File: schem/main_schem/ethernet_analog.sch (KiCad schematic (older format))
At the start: 11 parts

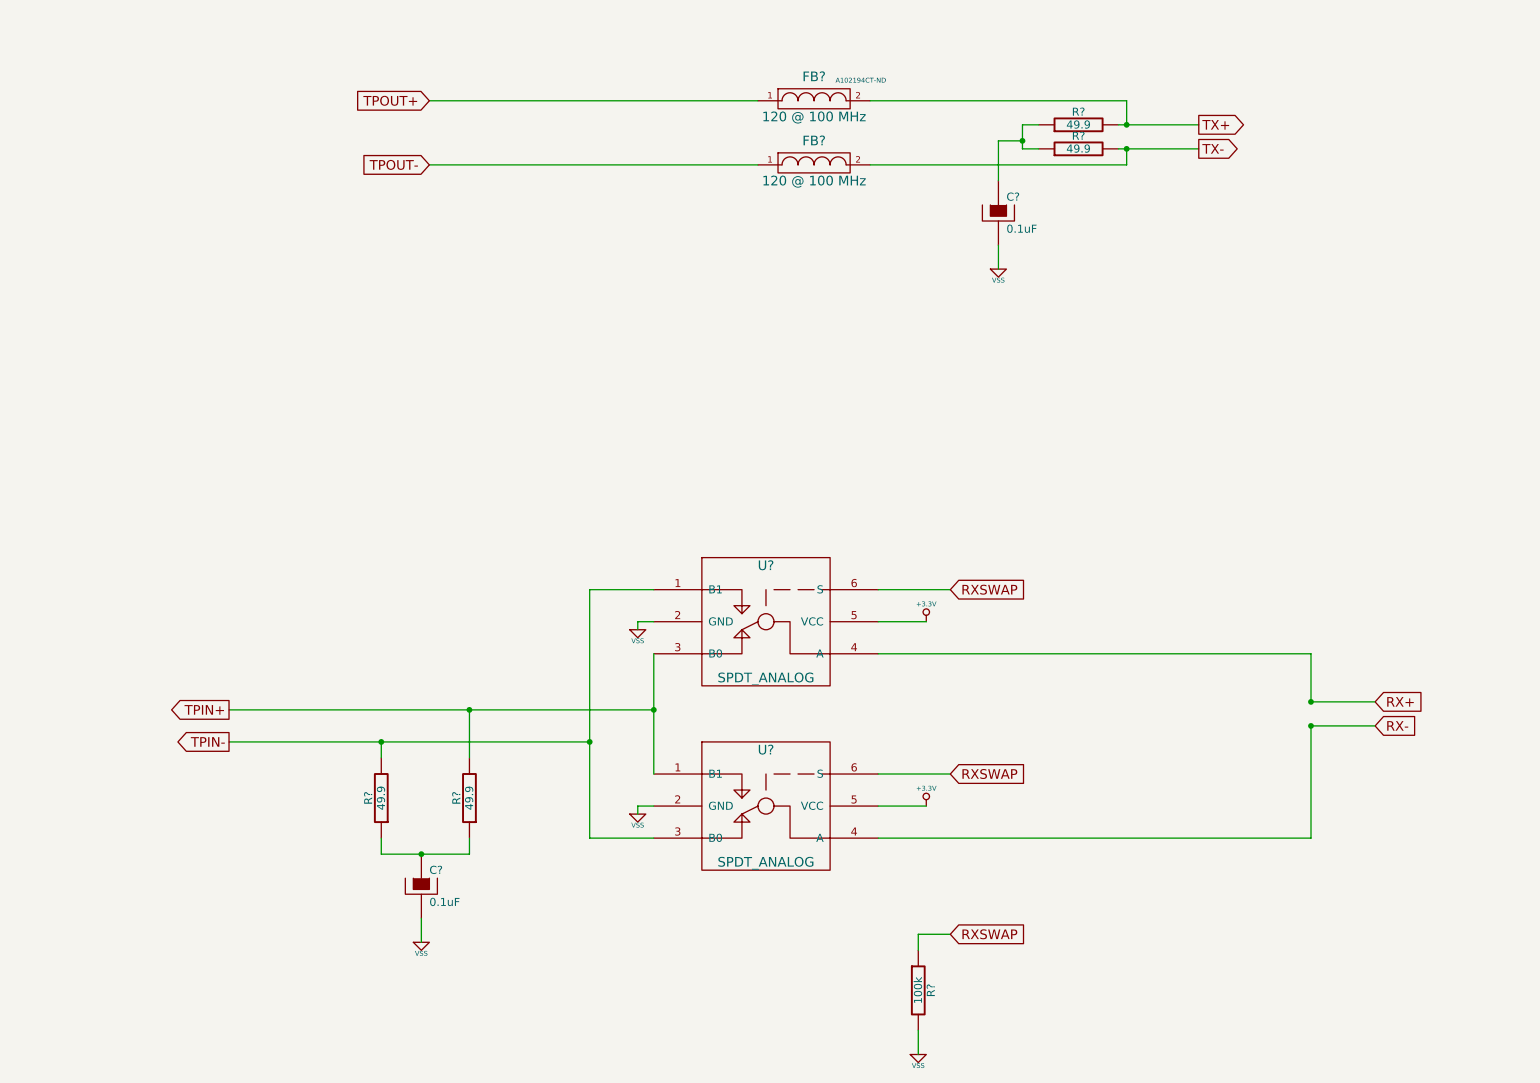
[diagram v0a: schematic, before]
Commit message: BOM sheets, update ethernet analog circuit
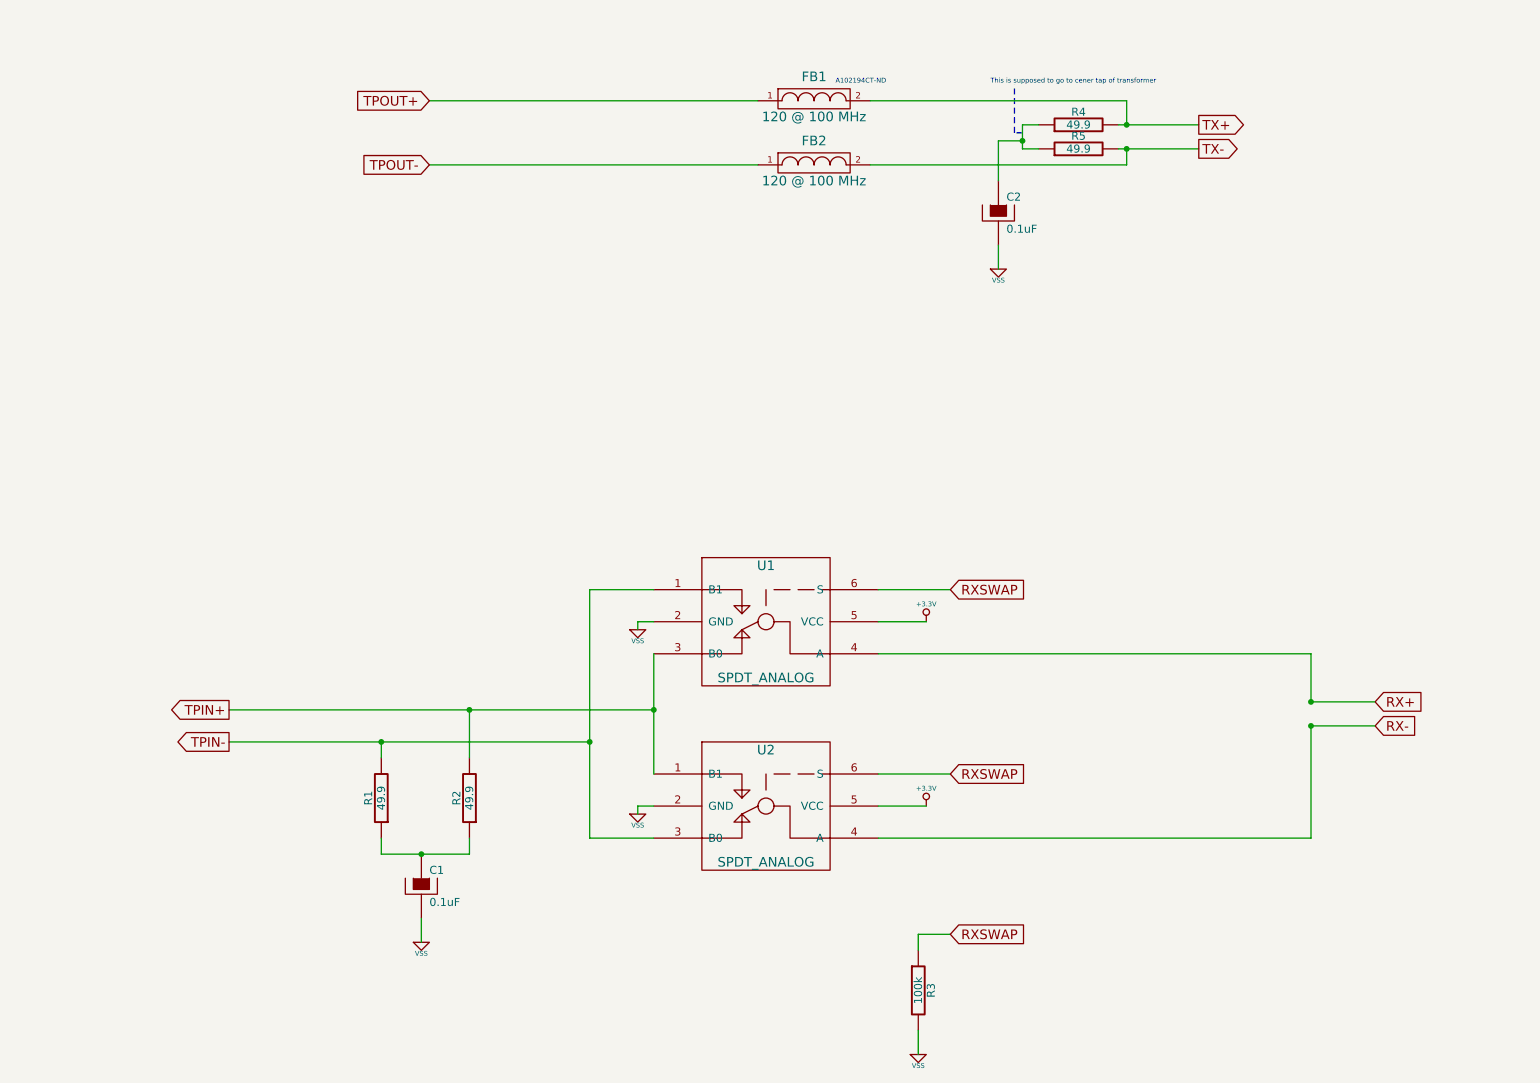
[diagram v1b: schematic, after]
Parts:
- gave numbers to parts that had none: 11
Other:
- note added: "This is supposed to go to cener tap of transformer"
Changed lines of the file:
@@
-EESchema Schematic File Version 2  date 10/5/2012 10:31:23 AM
+EESchema Schematic File Version 2  date 10/5/2012 11:52:46 PM
 LIBS:power
 LIBS:device
@@
 encoding utf-8
 Sheet 2 6
-Title ""
-Date "5 oct 2012"
+Title "Ethernet Analog Subsystem w/ Polarity Switching"
+Date "6 oct 2012"
 Rev ""
-Comp ""
-Comment1 ""
+Comp "Ingersoll Rand 402 Group"
+Comment1 "Brock Anderson, 2012"
 Comment2 ""
 Comment3 ""
 Comment4 ""
 $EndDescr
-$Comp
-L VSS #PWR?
+Wire Notes Line
+	7450 1250 7400 1250
+Wire Notes Line
+	7400 1250 7400 950
+Connection ~ 3700 5750
+Wire Wire Line
+	4000 5650 4000 5750
+Wire Wire Line
+	4000 5750 3450 5750
+Connection ~ 4000 4850
+Wire Wire Line
+	4000 5150 4000 4850
+Wire Wire Line
+	9650 4950 9250 4950
+Connection ~ 4750 5050
+Wire Wire Line
+	5150 4100 4750 4100
+Wire Wire Line
+	4750 4100 4750 5650
+Connection ~ 5150 4850
+Wire Wire Line
+	5150 5250 5150 4500
+Connection ~ 9250 4950
+Wire Wire Line
+	9250 4950 9250 5650
+Wire Wire Line
+	9250 5650 6550 5650
+Wire Wire Line
+	7000 6250 6800 6250
+Wire Wire Line
+	6800 6250 6800 6350
+Wire Wire Line
+	6550 5250 7000 5250
+Wire Wire Line
+	5050 4350 5050 4300
+Wire Wire Line
+	5050 4300 5150 4300
+Wire Wire Line
+	6550 5450 6850 5450
+Connection ~ 7450 1300
+Wire Wire Line
+	7450 1200 7450 1350
+Wire Wire Line
+	7450 1200 7550 1200
+Wire Wire Line
+	7300 1950 7300 2100
+Wire Wire Line
+	3750 1450 5800 1450
+Connection ~ 8100 1200
+Wire Wire Line
+	8100 1200 8100 1050
+Wire Wire Line
+	8100 1050 6500 1050
+Wire Wire Line
+	8050 1200 8550 1200
+Wire Wire Line
+	8050 1350 8550 1350
+Wire Wire Line
+	6500 1450 8100 1450
+Wire Wire Line
+	8100 1450 8100 1350
+Connection ~ 8100 1350
+Wire Wire Line
+	3750 1050 5800 1050
+Wire Wire Line
+	7300 1550 7300 1300
+Wire Wire Line
+	7300 1300 7450 1300
+Wire Wire Line
+	7450 1350 7550 1350
+Wire Wire Line
+	6550 4300 6850 4300
+Wire Wire Line
+	5050 5500 5050 5450
+Wire Wire Line
+	5050 5450 5150 5450
+Wire Wire Line
+	6550 4100 7000 4100
+Wire Wire Line
+	6800 6850 6800 7000
+Wire Wire Line
+	6550 4500 9250 4500
+Wire Wire Line
+	9250 4500 9250 4800
+Connection ~ 9250 4800
+Wire Wire Line
+	5150 4850 2500 4850
+Wire Wire Line
+	4750 5050 2500 5050
+Wire Wire Line
+	4750 5650 5150 5650
+Wire Wire Line
+	9250 4800 9650 4800
+Wire Wire Line
+	3450 5150 3450 5050
+Connection ~ 3450 5050
+Wire Wire Line
+	3450 5750 3450 5650
+Wire Wire Line
+	3700 6150 3700 6300
+Text Notes 7250 950  0    30   ~ 0
+This is supposed to go to cener tap of transformer
+$Comp
+L VSS #PWR01
 U 1 1 506EFD34
 P 7300 2100
-F 0 "#PWR?" H 7300 2100 30  0001 C CNN
+F 0 "#PWR01" H 7300 2100 30  0001 C CNN
 F 1 "VSS" H 7300 2030 30  0000 C CNN
 	1    7300 2100
 	1    0    0    -1
 $EndComp
-Wire Wire Line
-	3700 6150 3700 6300
-Wire Wire Line
-	3450 5650 3450 5750
-Connection ~ 3450 5050
-Wire Wire Line
-	3450 5150 3450 5050
-Wire Wire Line
-	9650 4800 9250 4800
-Wire Wire Line
-	5150 5650 4750 5650
-Wire Wire Line
-	4750 5050 2500 5050
-Wire Wire Line
-	5150 4850 2500 4850
-Connection ~ 9250 4800
-Wire Wire Line
-	9250 4800 9250 4500
-Wire Wire Line
-	9250 4500 6550 4500
-Wire Wire Line
-	6800 6850 6800 7000
-Wire Wire Line
-	6550 4100 7000 4100
-Wire Wire Line
-	5150 5450 5050 5450
-Wire Wire Line
-	5050 5450 5050 5500
-Wire Wire Line
-	6550 4300 6850 4300
-Wire Wire Line
-	7550 1350 7450 1350
-Wire Wire Line
-	7450 1300 7300 1300
-Wire Wire Line
-	7300 1300 7300 1550
-Wire Wire Line
-	3750 1050 5800 1050
-Connection ~ 8100 1350
-Wire Wire Line
-	8100 1350 8100 1450
-Wire Wire Line
-	8100 1450 6500 1450
-Wire Wire Line
-	8050 1350 8550 1350
-Wire Wire Line
-	8050 1200 8550 1200
-Wire Wire Line
-	6500 1050 8100 1050
-Wire Wire Line
-	8100 1050 8100 1200
-Connection ~ 8100 1200
-Wire Wire Line
-	3750 1450 5800 1450
-Wire Wire Line
-	7300 1950 7300 2100
-Wire Wire Line
-	7550 1200 7450 1200
-Wire Wire Line
-	7450 1200 7450 1350
-Connection ~ 7450 1300
-Wire Wire Line
-	6550 5450 6850 5450
-Wire Wire Line
-	5150 4300 5050 4300
-Wire Wire Line
-	5050 4300 5050 4350
-Wire Wire Line
-	6550 5250 7000 5250
-Wire Wire Line
-	6800 6350 6800 6250
-Wire Wire Line
-	6800 6250 7000 6250
-Wire Wire Line
-	6550 5650 9250 5650
-Wire Wire Line
-	9250 5650 9250 4950
-Connection ~ 9250 4950
-Wire Wire Line
-	5150 5250 5150 4500
-Connection ~ 5150 4850
-Wire Wire Line
-	4750 5650 4750 4100
-Wire Wire Line
-	4750 4100 5150 4100
-Connection ~ 4750 5050
-Wire Wire Line
-	9250 4950 9650 4950
-Wire Wire Line
-	4000 5150 4000 4850
-Connection ~ 4000 4850
-Wire Wire Line
-	3450 5750 4000 5750
-Wire Wire Line
-	4000 5750 4000 5650
-Connection ~ 3700 5750
-$Comp
-L CP C?
+$Comp
+L CP C1
 U 1 1 506EFD16
 P 3700 5950
-F 0 "C?" H 3750 6050 50  0000 L CNN
+F 0 "C1" H 3750 6050 50  0000 L CNN
 F 1 "0.1uF" H 3750 5850 50  0000 L CNN
 	1    3700 5950
@@
 $EndComp
 $Comp
-L VSS #PWR?
+L VSS #PWR02
 U 1 1 506EFD0E
 P 3700 6300
-F 0 "#PWR?" H 3700 6300 30  0001 C CNN
+F 0 "#PWR02" H 3700 6300 30  0001 C CNN
 F 1 "VSS" H 3700 6230 30  0000 C CNN
 	1    3700 6300
@@
 $EndComp
 $Comp
-L VSS #PWR?
+L VSS #PWR03
 U 1 1 506EFADF
 P 6800 7000
-F 0 "#PWR?" H 6800 7000 30  0001 C CNN
+F 0 "#PWR03" H 6800 7000 30  0001 C CNN
 F 1 "VSS" H 6800 6930 30  0000 C CNN
 	1    6800 7000
@@
 $EndComp
 $Comp
-L R R?
+L R R3
 U 1 1 506EFAD8
 P 6800 6600
-F 0 "R?" V 6880 6600 50  0000 C CNN
+F 0 "R3" V 6880 6600 50  0000 C CNN
 F 1 "100k" V 6800 6600 50  0000 C CNN
 	1    6800 6600
@@
 RXSWAP
 $Comp
-L VSS #PWR?
+L VSS #PWR04
 U 1 1 506EFA1F
 P 5050 4350
-F 0 "#PWR?" H 5050 4350 30  0001 C CNN
+F 0 "#PWR04" H 5050 4350 30  0001 C CNN
 F 1 "VSS" H 5050 4280 30  0000 C CNN
 	1    5050 4350
@@
 $EndComp
 $Comp
-L VSS #PWR?
+L VSS #PWR05
 U 1 1 506EF9D4
 P 5050 5500
-F 0 "#PWR?" H 5050 5500 30  0001 C CNN
+F 0 "#PWR05" H 5050 5500 30  0001 C CNN
 F 1 "VSS" H 5050 5430 30  0000 C CNN
 	1    5050 5500
@@
 $EndComp
 $Comp
-L +3.3V #PWR?
+L +3.3V #PWR06
 U 1 1 506EF9AE
 P 6850 5450
-F 0 "#PWR?" H 6850 5410 30  0001 C CNN
+F 0 "#PWR06" H 6850 5410 30  0001 C CNN
 F 1 "+3.3V" H 6850 5560 30  0000 C CNN
 	1    6850 5450
@@
 $EndComp
 $Comp
-L +3.3V #PWR?
+L +3.3V #PWR07
 U 1 1 506EF99F
 P 6850 4300
-F 0 "#PWR?" H 6850 4260 30  0001 C CNN
+F 0 "#PWR07" H 6850 4260 30  0001 C CNN
 F 1 "+3.3V" H 6850 4410 30  0000 C CNN
 	1    6850 4300
@@
 $EndComp
 $Comp
-L SPDT_ANALOG U?
+L SPDT_ANALOG U2
 U 1 1 506EF954
 P 5850 5400
-F 0 "U?" H 5850 5700 60  0000 C CNN
+F 0 "U2" H 5850 5700 60  0000 C CNN
 F 1 "SPDT_ANALOG" H 5850 5000 60  0000 C CNN
 	1    5850 5400
@@
 $EndComp
 $Comp
-L SPDT_ANALOG U?
+L SPDT_ANALOG U1
 U 1 1 506EF94B
 P 5850 4250
-F 0 "U?" H 5850 4550 60  0000 C CNN
+F 0 "U1" H 5850 4550 60  0000 C CNN
 F 1 "SPDT_ANALOG" H 5850 3850 60  0000 C CNN
 	1    5850 4250
@@
 $EndComp
 $Comp
-L CP C?
+L CP C2
 U 1 1 506EF466
 P 7300 1750
-F 0 "C?" H 7350 1850 50  0000 L CNN
+F 0 "C2" H 7350 1850 50  0000 L CNN
 F 1 "0.1uF" H 7350 1650 50  0000 L CNN
 	1    7300 1750
@@
 A102194CT-ND
 $Comp
-L FILTER FB?
+L FILTER FB2
 U 1 1 506EF3B9
 P 6150 1450
-F 0 "FB?" H 6150 1600 60  0000 C CNN
+F 0 "FB2" H 6150 1600 60  0000 C CNN
 F 1 "120 @ 100 MHz" H 6150 1350 60  0000 C CNN
 	1    6150 1450
@@
 $EndComp
 $Comp
-L FILTER FB?
+L FILTER FB1
 U 1 1 506EF3AF
 P 6150 1050
-F 0 "FB?" H 6150 1200 60  0000 C CNN
+F 0 "FB1" H 6150 1200 60  0000 C CNN
 F 1 "120 @ 100 MHz" H 6150 950 60  0000 C CNN
 	1    6150 1050
@@
 $EndComp
 $Comp
-L R R?
+L R R5
 U 1 1 506EEDA5
 P 7800 1350
-F 0 "R?" V 7880 1350 50  0000 C CNN
+F 0 "R5" V 7880 1350 50  0000 C CNN
 F 1 "49.9" V 7800 1350 50  0000 C CNN
 	1    7800 1350
@@
 $EndComp
 $Comp
-L R R?
+L R R4
 U 1 1 506EED9D
 P 7800 1200
-F 0 "R?" V 7880 1200 50  0000 C CNN
+F 0 "R4" V 7880 1200 50  0000 C CNN
 F 1 "49.9" V 7800 1200 50  0000 C CNN
 	1    7800 1200
@@
 $EndComp
 $Comp
-L R R?
+L R R2
 U 1 1 506EED96
 P 4000 5400
-F 0 "R?" V 4080 5400 50  0000 C CNN
+F 0 "R2" V 4080 5400 50  0000 C CNN
 F 1 "49.9" V 4000 5400 50  0000 C CNN
 	1    4000 5400
@@
 $EndComp
 $Comp
-L R R?
+L R R1
 U 1 1 506EED8E
 P 3450 5400
-F 0 "R?" V 3530 5400 50  0000 C CNN
+F 0 "R1" V 3530 5400 50  0000 C CNN
 F 1 "49.9" V 3450 5400 50  0000 C CNN
 	1    3450 5400

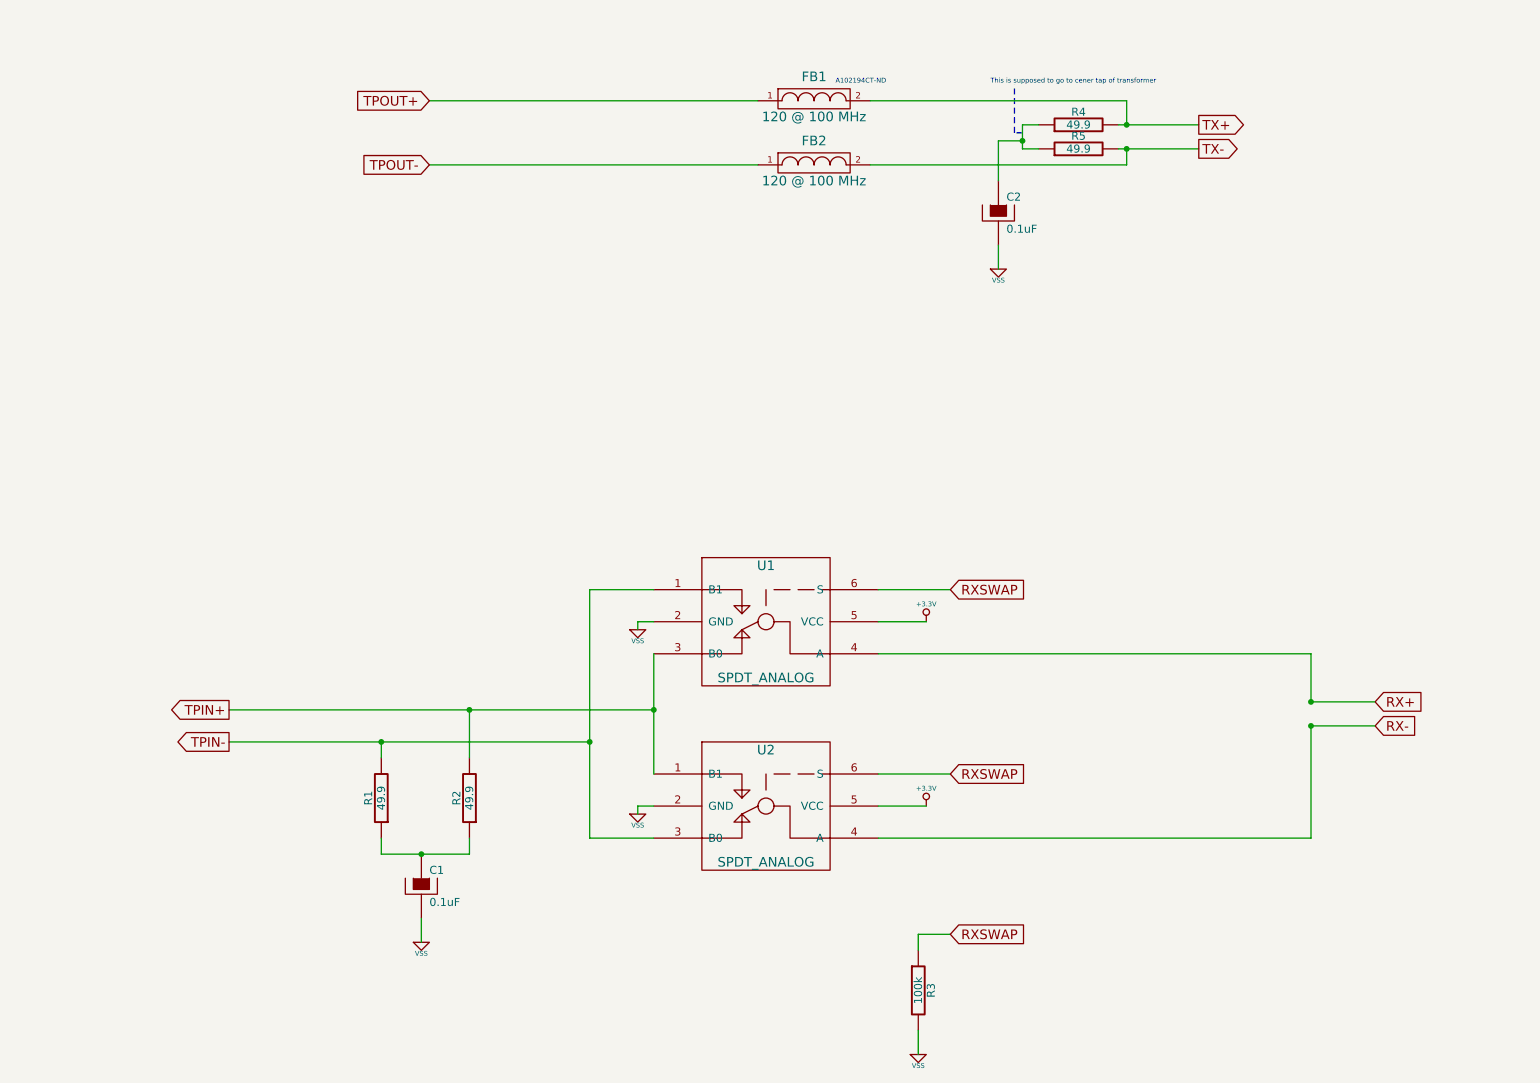
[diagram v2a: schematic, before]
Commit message: Update schematic to reflect backed up edits
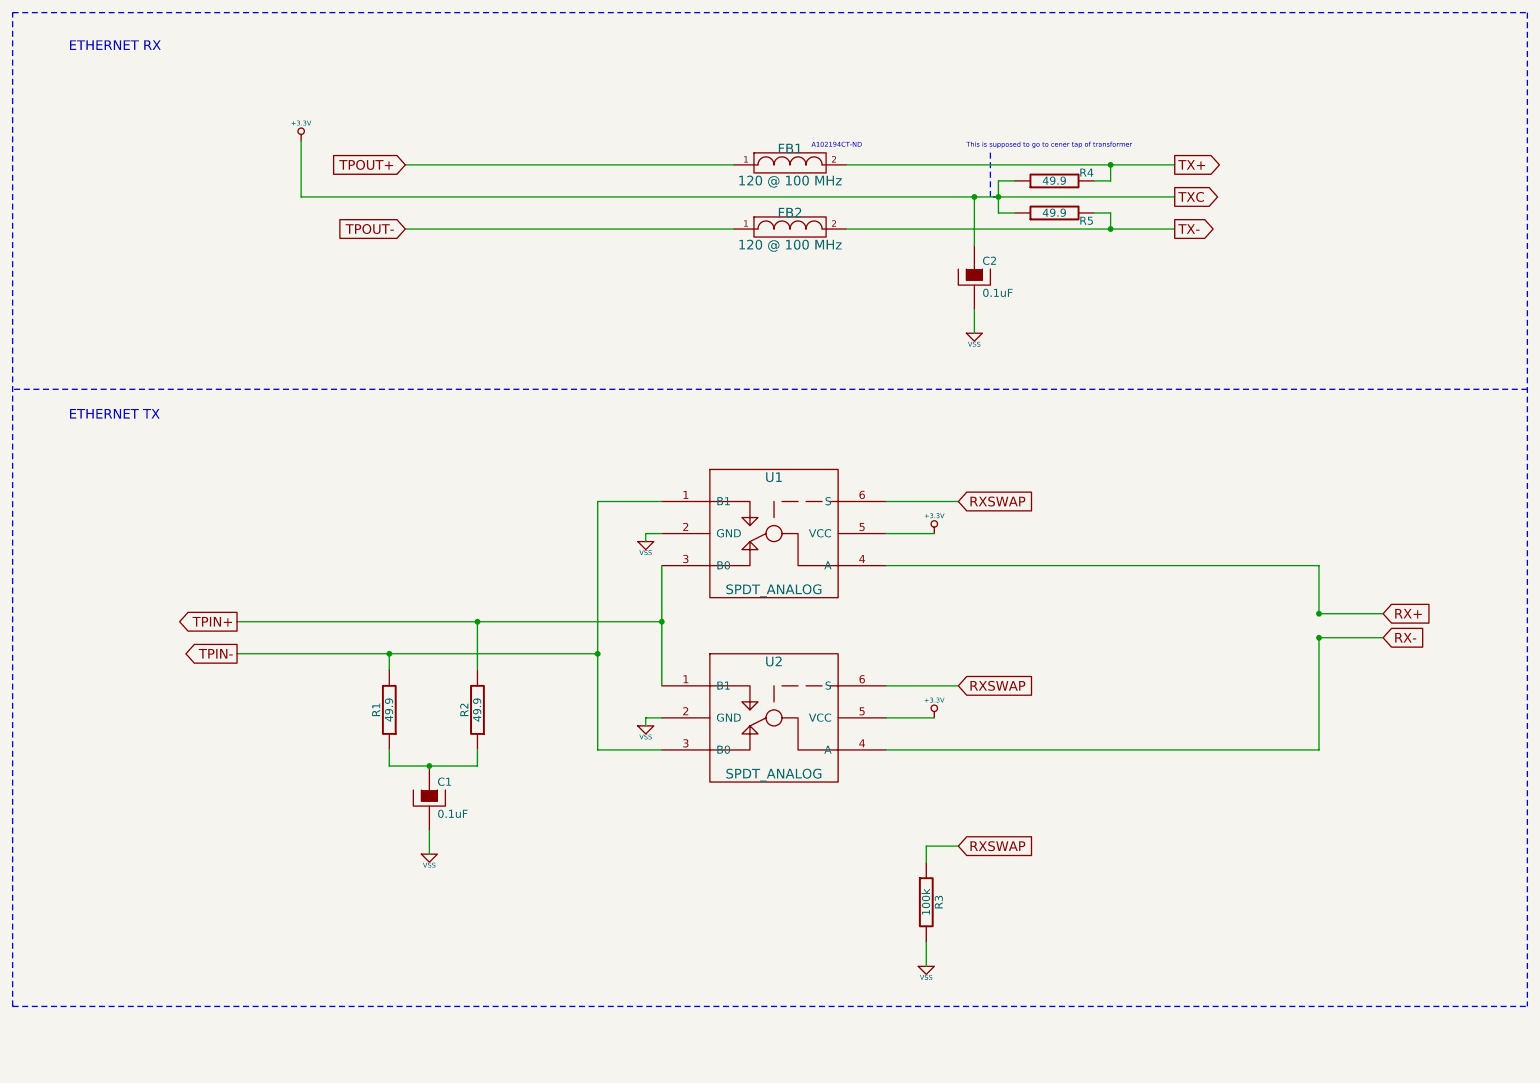
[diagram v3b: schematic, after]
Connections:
- net +3.3V: now also C2.1, R4.1, R5.1
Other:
- note added: "ETHERNET RX"
- note added: "ETHERNET TX"
- moved on the sheet: C1, C2, FB1, FB2, R1, R2, R3, R4, R5, U1, U2
